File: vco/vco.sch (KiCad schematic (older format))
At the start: 42 parts, among them J1 Power, J13 Octave, U1 TL074, U2 TL072, U3 AS3340, U4 LM4040

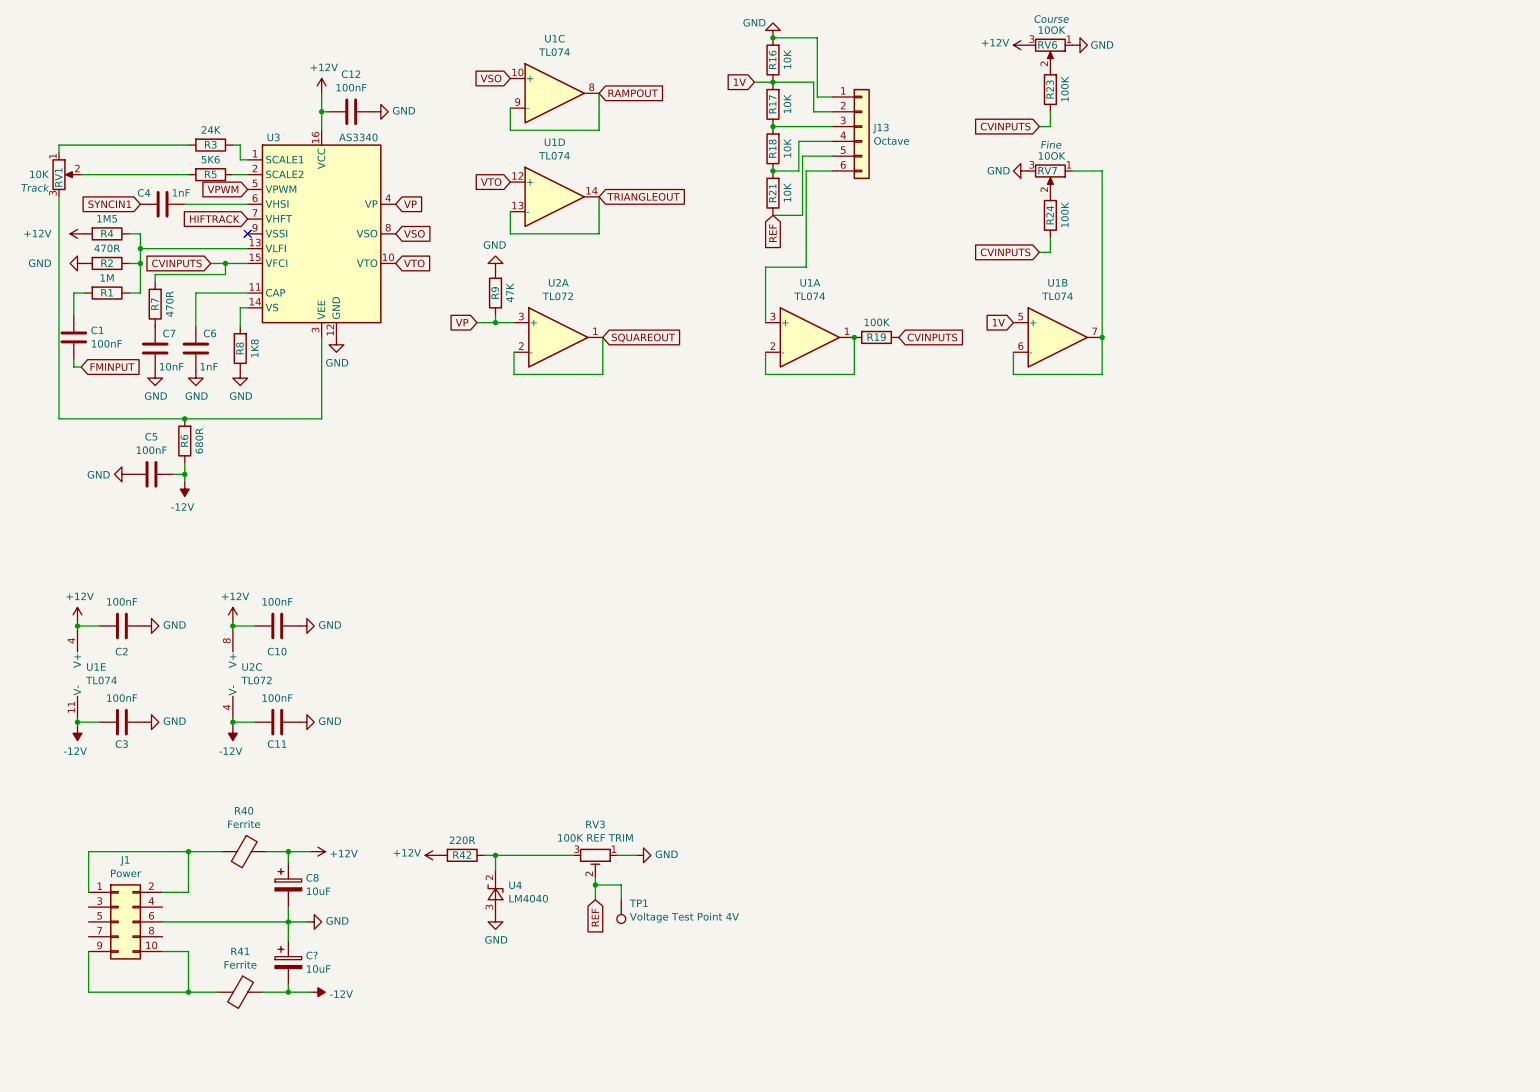
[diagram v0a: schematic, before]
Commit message: Add europower module that filters power and finish vco schamatics
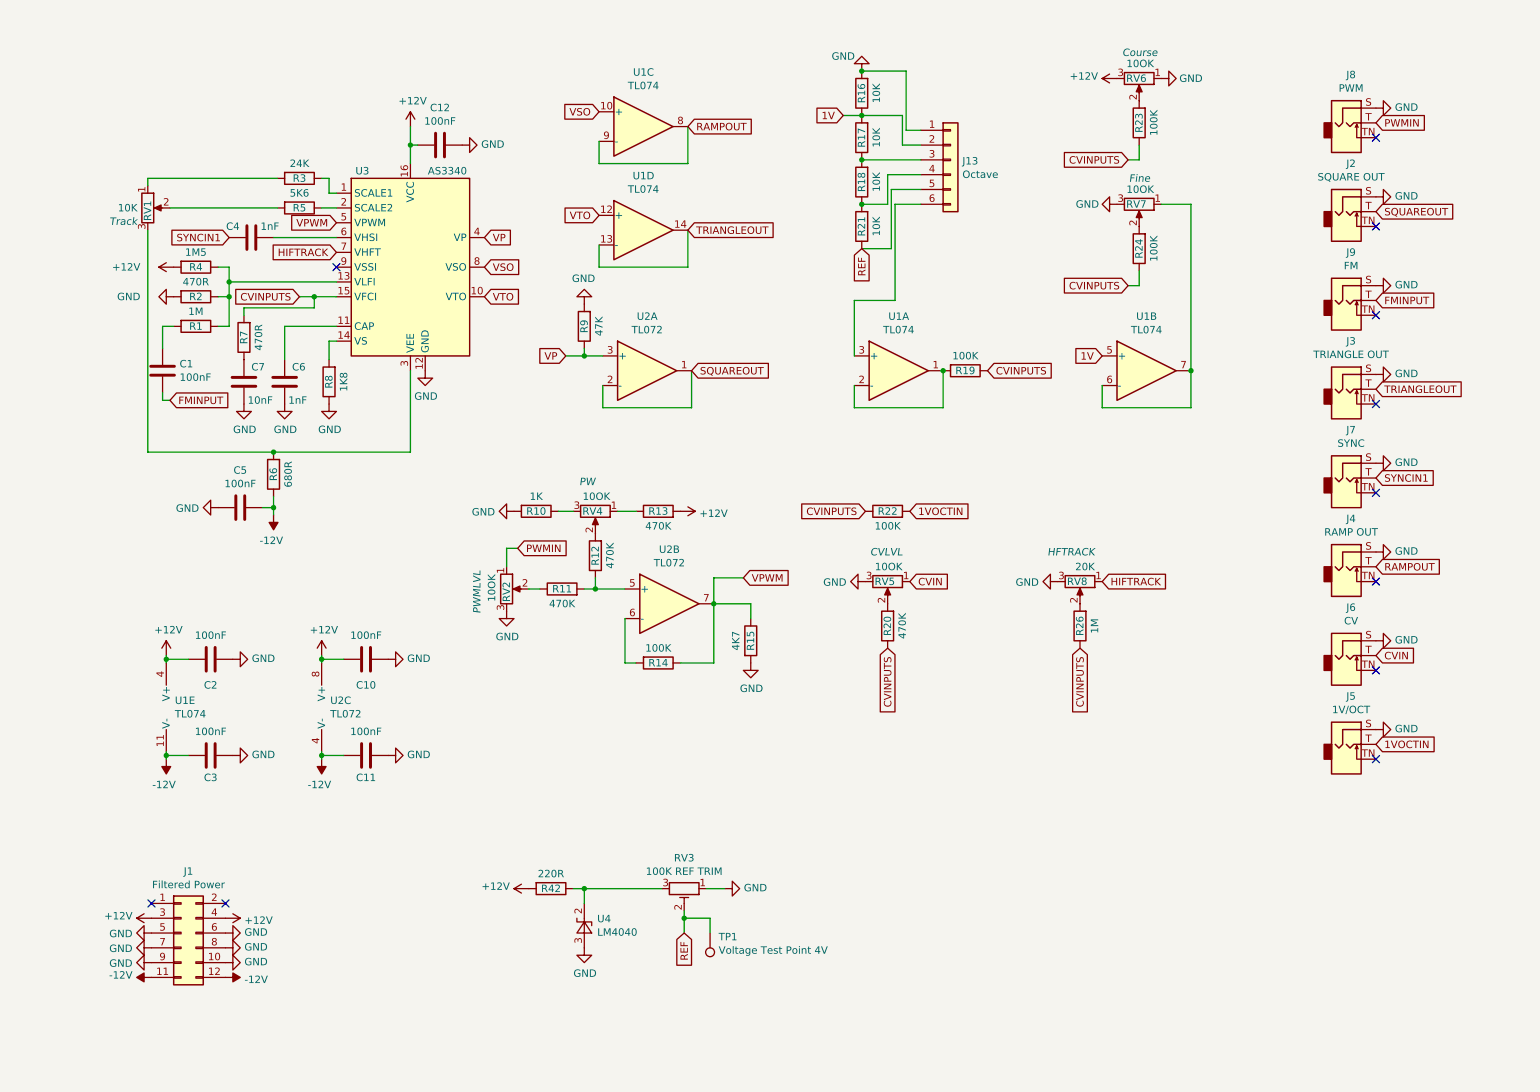
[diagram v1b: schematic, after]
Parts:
- removed C8, C?: 10uF, Capacitor_THT:CP_Radial_D5.0mm_P2.50mm, symbol Device:CP
- removed J1: Power, symbol Connector_Generic:Conn_02x05_Odd_Even
- removed R40, R41: Ferrite, symbol Device:Ferrite_Bead
- added J1: Filtered Power, Connector_PinSocket_2.54mm:PinSocket_2x06_P2.54mm_Vertical, symbol Connector_Generic:Conn_02x06_Odd_Even
- added J2: SQUARE OUT, Connector_Audio:Jack_3.5mm_QingPu_WQP-PJ398SM_Vertical_CircularHoles, symbol Connector:AudioJack2_SwitchT
- added J3: TRIANGLE OUT, Connector_Audio:Jack_3.5mm_QingPu_WQP-PJ398SM_Vertical_CircularHoles, symbol Connector:AudioJack2_SwitchT
- added J4: RAMP OUT, Connector_Audio:Jack_3.5mm_QingPu_WQP-PJ398SM_Vertical_CircularHoles, symbol Connector:AudioJack2_SwitchT
- added J5: 1V/OCT, Connector_Audio:Jack_3.5mm_QingPu_WQP-PJ398SM_Vertical_CircularHoles, symbol Connector:AudioJack2_SwitchT
- added J6: CV, Connector_Audio:Jack_3.5mm_QingPu_WQP-PJ398SM_Vertical_CircularHoles, symbol Connector:AudioJack2_SwitchT
- added J7: SYNC, Connector_Audio:Jack_3.5mm_QingPu_WQP-PJ398SM_Vertical_CircularHoles, symbol Connector:AudioJack2_SwitchT
- added J8: PWM, Connector_Audio:Jack_3.5mm_QingPu_WQP-PJ398SM_Vertical_CircularHoles, symbol Connector:AudioJack2_SwitchT
- added J9: FM, Connector_Audio:Jack_3.5mm_QingPu_WQP-PJ398SM_Vertical_CircularHoles, symbol Connector:AudioJack2_SwitchT
- added R10: 1K, Resistor_THT:R_Axial_DIN0207_L6.3mm_D2.5mm_P7.62mm_Horizontal, symbol Device:R
- added R11, R12, R13, R20: 470K, Resistor_THT:R_Axial_DIN0207_L6.3mm_D2.5mm_P7.62mm_Horizontal, symbol Device:R
- added R14, R22: 100K, Resistor_THT:R_Axial_DIN0207_L6.3mm_D2.5mm_P7.62mm_Horizontal, symbol Device:R
- added R15: 4K7, Resistor_THT:R_Axial_DIN0207_L6.3mm_D2.5mm_P7.62mm_Horizontal, symbol Device:R
- added R26: 1M, Resistor_THT:R_Axial_DIN0207_L6.3mm_D2.5mm_P7.62mm_Horizontal, symbol Device:R
- added RV2, RV4, RV5: 10OK, Potentiometer_THT:Potentiometer_Alps_RK09L_Single_Vertical, symbol Device:R_POT
- added RV8: 20K, Potentiometer_THT:Potentiometer_Alps_RK09L_Single_Vertical, symbol Device:R_POT
- added unit 2 of U2
- J13: footprint (none) -> Connector_PinHeader_2.54mm:PinHeader_1x06_P2.54mm_Vertical
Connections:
- net +12V: now also J1.3 (Pin_3), J1.4 (Pin_4), R13.2
- net -12V: now also J1.11 (Pin_11), J1.12 (Pin_12)
- net CVINPUTS: now also R20.1, R22.1, R26.1
- net FMINPUT: now also J9.T
- net GND: now also J1.10 (Pin_10), J1.5 (Pin_5), J1.6 (Pin_6), J1.7 (Pin_7), J1.8 (Pin_8), J1.9 (Pin_9), J2.S, J3.S, J4.S, J5.S, J6.S, J7.S, J8.S, J9.S, R10.2, R15.2, RV2.3, RV5.3, RV8.3
- net HIFTRACK: now also RV8.1
- net RAMPOUT: now also J4.T
- net SQUAREOUT: now also J2.T
- net SYNCIN1: now also J7.T
- net TRIANGLEOUT: now also J3.T
- net VPWM: now also R14.1, R15.1, U2.7
- new net: R11.2, R12.1, U2.5 (+)
- new net: R14.2, U2.6 (-)
- new net: R13.1, RV4.1
- new net: R12.2, RV4.2
- new net: R10.1, RV4.3
- new net: R11.1, RV2.2
- new net: R20.2, RV5.2
- new net: R26.2, RV8.2
- new net 1VOCTIN: J5.T, R22.2
- new net CVIN: J6.T, RV5.1
- new net PWMIN: J8.T, RV2.1
- no-connect marks 1 -> 11
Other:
- moved on the sheet: C1, C10, C11, C12, C2, C3, C4, C5, C6, C7, J13, R1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

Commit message: Increase trace width on brain, start sorting stuff for vco and start writing shopping list
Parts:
- RV1, RV8: footprint Potentiometer_THT:Potentiometer_Alps_RK09L_Single_Vertical -> Connector_PinHeader_2.54mm:PinHeader_1x03_P2.54mm_Vertical
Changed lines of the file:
@@
 F 0 "RV1" V 1375 1875 50  0000 R CNN
 F 1 "10K" H 1305 1825 50  0000 R CNN
-F 2 "Potentiometer_THT:Potentiometer_Alps_RK09L_Single_Vertical" H 1375 1825 50  0001 C CNN
+F 2 "Connector_PinHeader_2.54mm:PinHeader_1x03_P2.54mm_Vertical" H 1375 1825 50  0001 C CNN
 F 3 "~" H 1375 1825 50  0001 C CNN
 F 4 "Track" H 1305 1734 50  0000 R CIN "Label"
@@
 F 0 "RV8" V 7675 4400 50  0000 R CNN
 F 1 "20K" V 7575 4450 50  0000 R CNN
-F 2 "Potentiometer_THT:Potentiometer_Alps_RK09L_Single_Vertical" H 7675 4350 50  0001 C CNN
+F 2 "Connector_PinHeader_2.54mm:PinHeader_1x03_P2.54mm_Vertical" H 7675 4350 50  0001 C CNN
 F 3 "~" H 7675 4350 50  0001 C CNN
 F 4 "HFTRACK" V 7475 4450 50  0000 R CIN "Label"

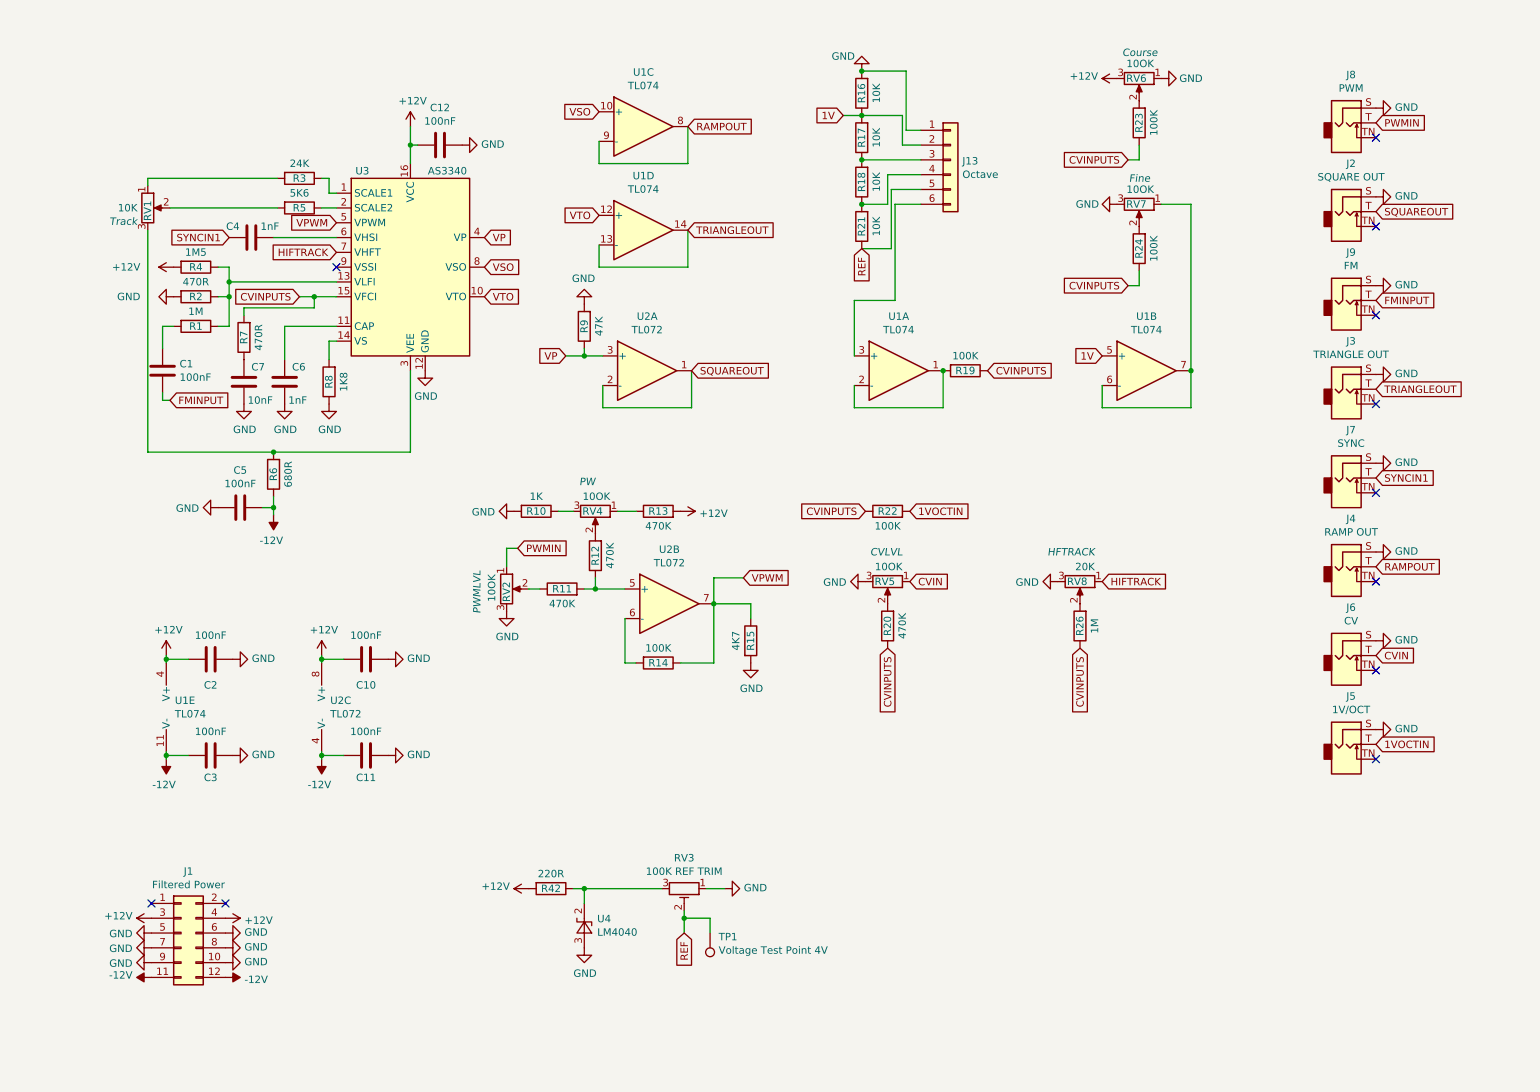
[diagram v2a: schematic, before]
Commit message: Extra 7805 footprint, new standard, and some order to the VCO chaos
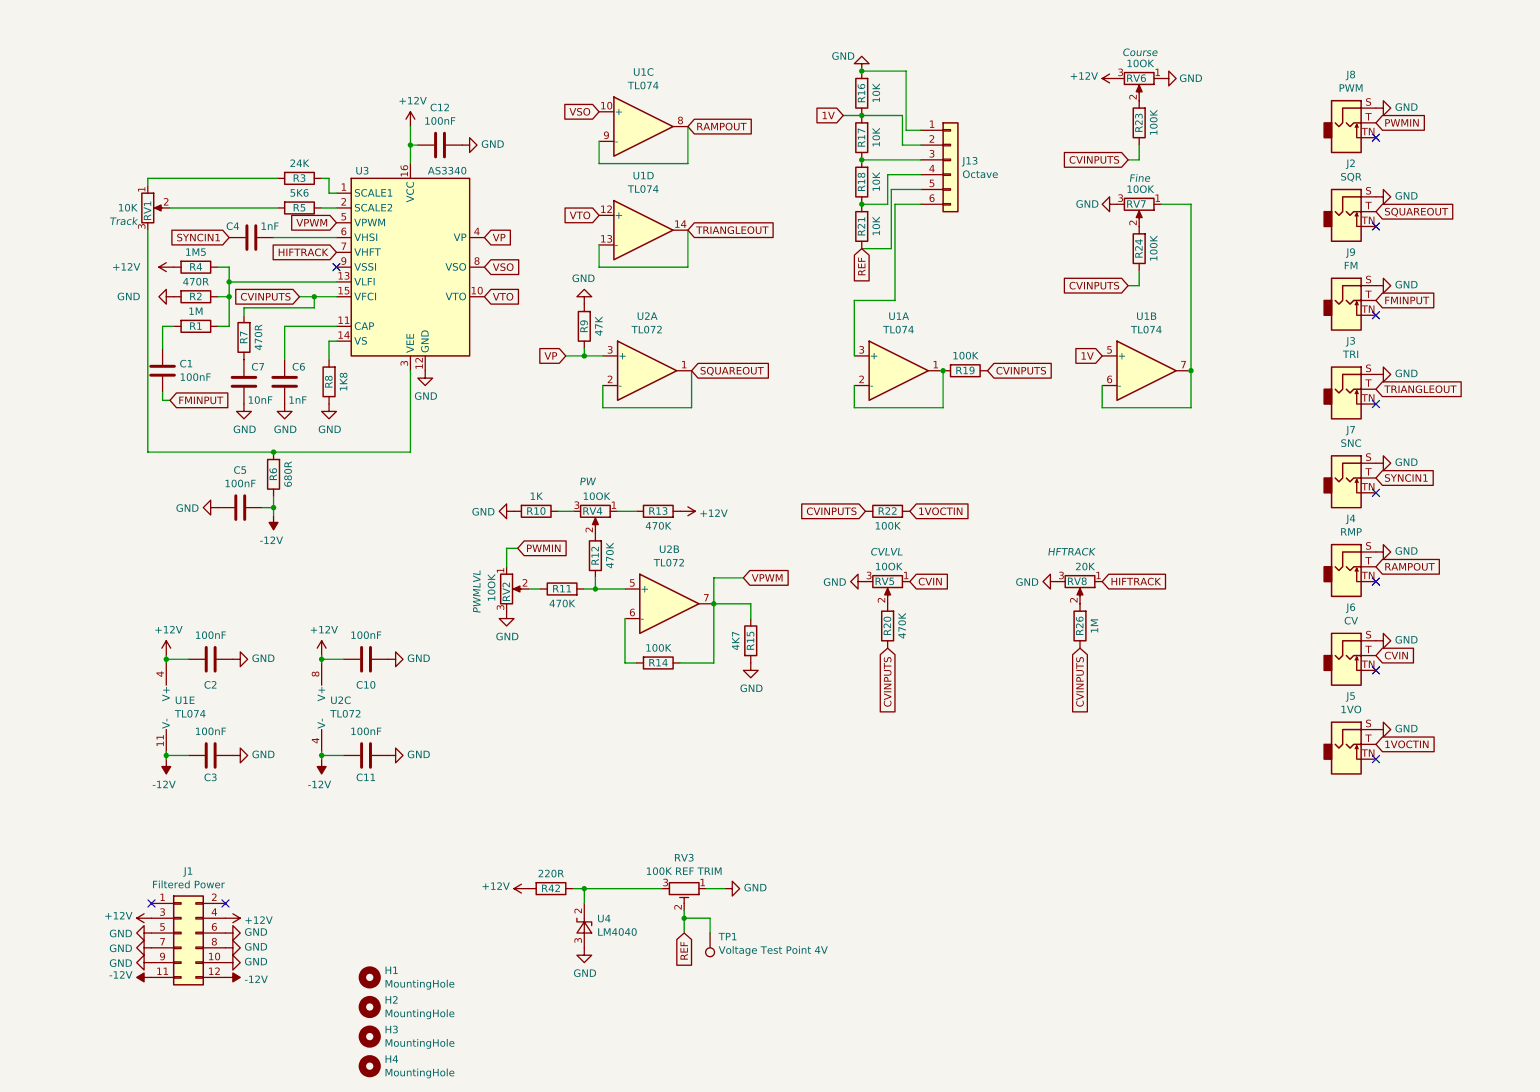
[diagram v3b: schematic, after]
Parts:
- added H1, H2, H3, H4: MountingHole, MountingHole:MountingHole_3.2mm_M3, symbol Mechanical:MountingHole
- J2: value SQUARE OUT -> SQR
- J3: value TRIANGLE OUT -> TRI
- J4: value RAMP OUT -> RMP
- J5: value 1V/OCT -> 1VO
- J7: value SYNC -> SNC
- R1, R10, R11, R12, R13, R14, R15, R16, R17, R18, R19, R2, R20, R21, R22, R23, R24, R26, R3, R4, R42, R5, R6, R7, R8, R9: footprint Resistor_THT:R_Axial_DIN0207_L6.3mm_D2.5mm_P7.62mm_Horizontal -> Resistor_THT:R_Axial_DIN0204_L3.6mm_D1.6mm_P7.62mm_Horizontal
- RV1, RV3, RV8: footprint Connector_PinHeader_2.54mm:PinHeader_1x03_P2.54mm_Vertical -> 3296W-1-250:TRIM_3296W-1-250
- RV5: footprint Potentiometer_THT:Potentiometer_Alps_RK09L_Single_Vertical -> 3296W-1-250:TRIM_3296W-1-250

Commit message: Settled at larger pcb, think its going to work with components placed like this
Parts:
- removed H2, H4: MountingHole, MountingHole:MountingHole_3.2mm_M3, symbol Mechanical:MountingHole
- U1: footprint Package_DIP:DIP-16_W7.62mm -> Package_DIP:DIP-14_W7.62mm_Socket
- U2: footprint Package_DIP:DIP-8_W7.62mm -> Package_DIP:DIP-8_W7.62mm_Socket
- U3: footprint Package_DIP:DIP-16_W7.62mm -> Package_DIP:DIP-16_W7.62mm_Socket
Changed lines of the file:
@@
 F 0 "U3" H 2825 2875 50  0000 C CNN
 F 1 "AS3340" H 3400 2875 50  0000 C CNN
-F 2 "Package_DIP:DIP-16_W7.62mm" H 3650 1925 50  0001 C CNN
+F 2 "Package_DIP:DIP-16_W7.62mm_Socket" H 3650 1925 50  0001 C CNN
 F 3 "http://www.alfarzpp.lv/eng/sc/AS3340.pdf" H 3750 1775 50  0001 C CNN
 	1    3150 2225
@@
 F 0 "U1" H 4725 1642 50  0000 C CNN
 F 1 "TL074" H 4725 1551 50  0000 C CNN
-F 2 "Package_DIP:DIP-16_W7.62mm" H 4675 1375 50  0001 C CNN
+F 2 "Package_DIP:DIP-14_W7.62mm_Socket" H 4675 1375 50  0001 C CNN
 F 3 "http://www.ti.com/lit/ds/symlink/tl071.pdf" H 4775 1475 50  0001 C CNN
 	3    4725 1275
@@
 F 0 "U1" H 4725 2342 50  0000 C CNN
 F 1 "TL074" H 4725 2251 50  0000 C CNN
-F 2 "Package_DIP:DIP-16_W7.62mm" H 4675 2075 50  0001 C CNN
+F 2 "Package_DIP:DIP-14_W7.62mm_Socket" H 4675 2075 50  0001 C CNN
 F 3 "http://www.ti.com/lit/ds/symlink/tl071.pdf" H 4775 2175 50  0001 C CNN
 	4    4725 1975
@@
 F 0 "U1" H 6450 3292 50  0000 C CNN
 F 1 "TL074" H 6450 3201 50  0000 C CNN
-F 2 "Package_DIP:DIP-16_W7.62mm" H 6400 3025 50  0001 C CNN
+F 2 "Package_DIP:DIP-14_W7.62mm_Socket" H 6400 3025 50  0001 C CNN
 F 3 "http://www.ti.com/lit/ds/symlink/tl071.pdf" H 6500 3125 50  0001 C CNN
 	1    6450 2925
@@
 F 0 "U1" H 8125 3292 50  0000 C CNN
 F 1 "TL074" H 8125 3201 50  0000 C CNN
-F 2 "Package_DIP:DIP-16_W7.62mm" H 8075 3025 50  0001 C CNN
+F 2 "Package_DIP:DIP-14_W7.62mm_Socket" H 8075 3025 50  0001 C CNN
 F 3 "http://www.ti.com/lit/ds/symlink/tl071.pdf" H 8175 3125 50  0001 C CNN
 	2    8125 2925
@@
 F 0 "U2" H 4750 3292 50  0000 C CNN
 F 1 "TL072" H 4750 3201 50  0000 C CNN
-F 2 "Package_DIP:DIP-8_W7.62mm" H 4700 3025 50  0001 C CNN
+F 2 "Package_DIP:DIP-8_W7.62mm_Socket" H 4700 3025 50  0001 C CNN
 F 3 "http://www.ti.com/lit/ds/symlink/tl071.pdf" H 4800 3125 50  0001 C CNN
 	1    4750 2925
@@
 F 0 "U1" H 1558 5246 50  0000 L CNN
 F 1 "TL074" H 1558 5155 50  0000 L CNN
-F 2 "Package_DIP:DIP-16_W7.62mm" H 1550 5300 50  0001 C CNN
+F 2 "Package_DIP:DIP-14_W7.62mm_Socket" H 1550 5300 50  0001 C CNN
 F 3 "http://www.ti.com/lit/ds/symlink/tl071.pdf" H 1650 5400 50  0001 C CNN
 	5    1600 5200
@@
 F 0 "U2" H 2608 5246 50  0000 L CNN
 F 1 "TL072" H 2608 5155 50  0000 L CNN
-F 2 "Package_DIP:DIP-8_W7.62mm" H 2600 5300 50  0001 C CNN
+F 2 "Package_DIP:DIP-8_W7.62mm_Socket" H 2600 5300 50  0001 C CNN
 F 3 "http://www.ti.com/lit/ds/symlink/tl071.pdf" H 2700 5400 50  0001 C CNN
 	3    2650 5200
@@
 F 0 "U2" H 4900 4867 50  0000 C CNN
 F 1 "TL072" H 4900 4776 50  0000 C CNN
-F 2 "Package_DIP:DIP-8_W7.62mm" H 4850 4600 50  0001 C CNN
+F 2 "Package_DIP:DIP-8_W7.62mm_Socket" H 4850 4600 50  0001 C CNN
 F 3 "http://www.ti.com/lit/ds/symlink/tl071.pdf" H 4950 4700 50  0001 C CNN
 	2    4900 4500
@@
 $EndComp
 $Comp
-L Mechanical:MountingHole H2
-U 1 1 5E216479
-P 2875 7225
-F 0 "H2" H 2975 7271 50  0000 L CNN
-F 1 "MountingHole" H 2975 7180 50  0000 L CNN
-F 2 "MountingHole:MountingHole_3.2mm_M3" H 2875 7225 50  0001 C CNN
-F 3 "~" H 2875 7225 50  0001 C CNN
-	1    2875 7225
-	1    0    0    -1
-$EndComp
-$Comp
 L Mechanical:MountingHole H3
 U 1 1 5E2169CD
@@
 	1    0    0    -1
 $EndComp
-$Comp
-L Mechanical:MountingHole H4
-U 1 1 5E216F3F
-P 2875 7625
-F 0 "H4" H 2975 7671 50  0000 L CNN
-F 1 "MountingHole" H 2975 7580 50  0000 L CNN
-F 2 "MountingHole:MountingHole_3.2mm_M3" H 2875 7625 50  0001 C CNN
-F 3 "~" H 2875 7625 50  0001 C CNN
-	1    2875 7625
-	1    0    0    -1
-$EndComp
